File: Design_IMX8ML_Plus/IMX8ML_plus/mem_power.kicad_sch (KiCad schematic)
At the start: 22 parts

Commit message: processor capacitors location
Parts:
- removed C2 (x12): 1uF, Capacitor_SMD:C_0201_0603Metric_Pad0.64x0.40mm_HandSolder, symbol Device:C_Small
- removed C2 (x4): 10uF, Capacitor_SMD:C_0402_1005Metric, symbol Device:C_Small
- added C2 (x13): 1uF, Capacitor_SMD:C_0201_0603Metric_Pad0.64x0.40mm_HandSolder, symbol Device:C_Small
- added C2 (x3): 10uF, Capacitor_SMD:C_0402_1005Metric, symbol Device:C_Small
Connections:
- net GND: now also C2.2, C2.2, C2.2, C2.2, C2.2, C2.2, C2.2, C2.2, C2.2, C2.2, C2.2, C2.2, C2.2, C2.2, C2.2, C2.2
- net LPD4_VDD1 renamed VDD_1V8
- new net NVCC_DRAM_1V1: C2.1, C2.1, C2.1, C2.1, C2.1, C2.1, C2.1, C2.1, C2.1, C2.1, C2.1, C2.1, C2.1, C2.1, C2.1, C2.1

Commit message: Add SPB228 WIFI/BLE module
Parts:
- renumbered C2 to C124, C2 to C125, C2 to C126, C2 to C127, C2 to C128, C2 to C129, C2 to C130, C2 to C131, C2 to C133, C2 to C134, C2 to C135, C2 to C136, C2 to C137, C2 to C138, C2 to C139, C2 to C140, C2 to C3, C2 to C4, C2 to C5, C2 to C6, C2 to C7, C2 to C8

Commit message: [PROCESSOR] Create zones It added power zones in the four layer
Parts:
- renumbered C5 to C30, C4 to C31, C3 to C32, C6 to C33, C7 to C34, C8 to C35, C124 to C36, C125 to C37, C126 to C38, C127 to C39, C128 to C40, C129 to C41, C130 to C42, C131 to C43, C133 to C44, C134 to C45, C135 to C46, C136 to C47, C137 to C48, C138 to C49, C139 to C50, C140 to C51

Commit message: [IMX8ML-CPU] LPDDR4 memories reorganization of track between processor and memories.
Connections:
- net NVCC_DRAM_1V1 renamed LP4_VDD2
- net VDD_1V8 renamed LP4_VDD1
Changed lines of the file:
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@@
+	)
+	(junction
+		(at 96.52 58.42)
+		(diameter 0)
+		(color 0 0 0 0)
 	)
 	(junction
@@
 	)
 	(junction
+		(at 209.55 102.87)
+		(diameter 0)
+		(color 0 0 0 0)
+	)
+	(junction
 		(at 69.85 58.42)
 		(diameter 0)
@@
 	)
 	(junction
+		(at 209.55 81.28)
+		(diameter 0)
+		(color 0 0 0 0)
+	)
+	(junction
 		(at 173.99 81.28)
 		(diameter 0)
@@
 	(wire
 		(pts
+			(xy 209.55 81.28) (xy 214.63 81.28)
+		)
+		(stroke
+			(width 0)
+			(type default)
+		)
+	)
+	(wire
+		(pts
 			(xy 209.55 111.76) (xy 209.55 114.3)
 		)
@@
 	(wire
 		(pts
+			(xy 212.09 102.87) (xy 209.55 102.87)
+		)
+		(stroke
+			(width 0)
+			(type default)
+		)
+	)
+	(wire
+		(pts
 			(xy 96.52 67.31) (xy 96.52 69.85)
 		)
@@
 	(wire
 		(pts
+			(xy 99.06 58.42) (xy 96.52 58.42)
+		)
+		(stroke
+			(width 0)
+			(type default)
+		)
+	)
+	(wire
+		(pts
 			(xy 87.63 67.31) (xy 87.63 69.85)
 		)
@@
 		)
 	)
+	(global_label "LP4_VDDQ"
+		(shape input)
+		(at 212.09 102.87 0)
+		(fields_autoplaced yes)
+		(effects
+			(font
+				(size 1 1)
+			)
+			(justify left)
+		)
+		(property "Intersheetrefs" "${INTERSHEET_REFS}"
+			(at 221.8688 102.87 0)
+			(effects
+				(font
+					(size 1.27 1.27)
+				)
+				(justify left)
+				(hide yes)
+			)
+		)
+	)
+	(global_label "LP4_VDD1"
+		(shape input)
+		(at 99.06 58.42 0)
+		(fields_autoplaced yes)
+		(effects
+			(font
+				(size 1 1)
+			)
+			(justify left)
+		)
+		(property "Intersheetrefs" "${INTERSHEET_REFS}"
+			(at 108.7436 58.42 0)
+			(effects
+				(font
+					(size 1.27 1.27)
+				)
+				(justify left)
+				(hide yes)
+			)
+		)
+	)
+	(global_label "LP4_VDD2"
+		(shape input)
+		(at 214.63 81.28 0)
+		(fields_autoplaced yes)
+		(effects
+			(font
+				(size 1 1)
+			)
+			(justify left)
+		)
+		(property "Intersheetrefs" "${INTERSHEET_REFS}"
+			(at 224.3136 81.28 0)
+			(effects
+				(font
+					(size 1.27 1.27)
+				)
+				(justify left)
+				(hide yes)
+			)
+		)
+	)

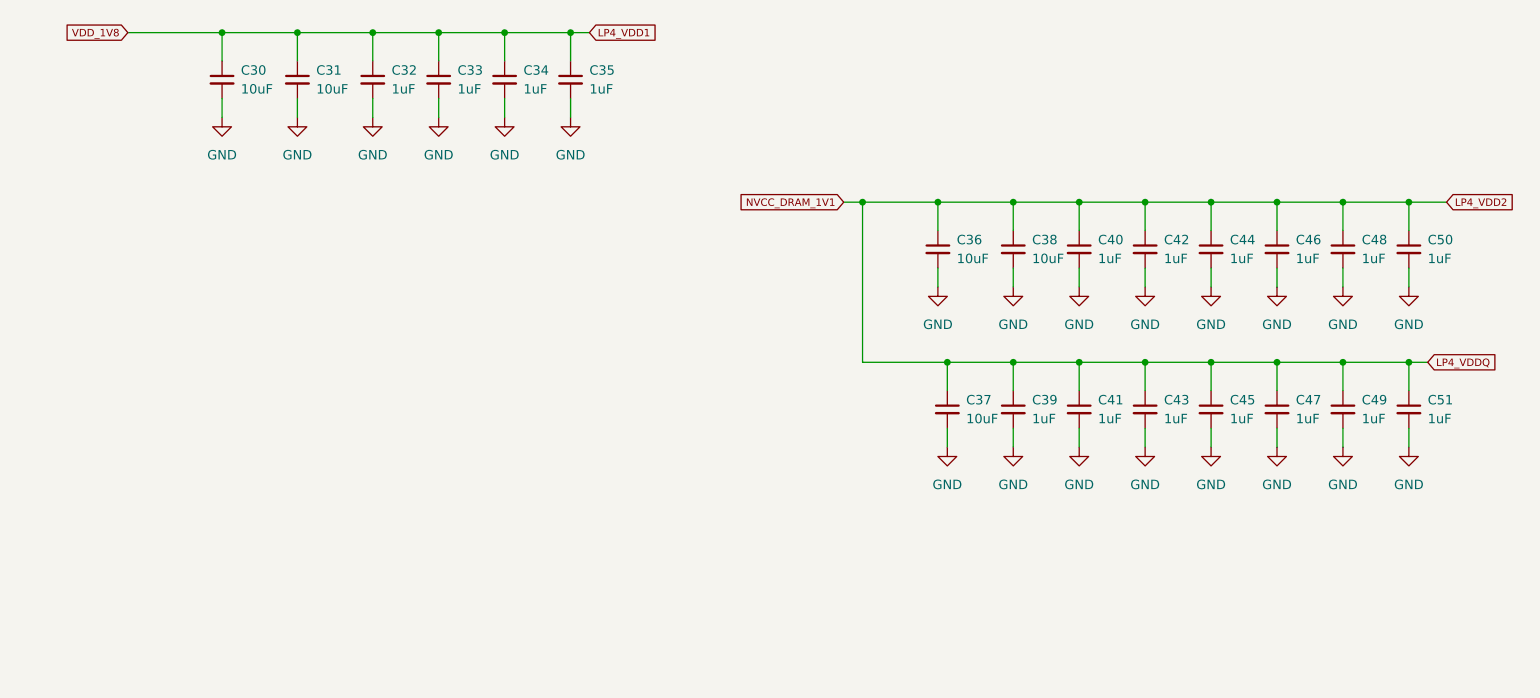
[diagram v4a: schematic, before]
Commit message: [BB_IMX8MLP IMX8MLP] Actuallizated to 9.0 kicad version
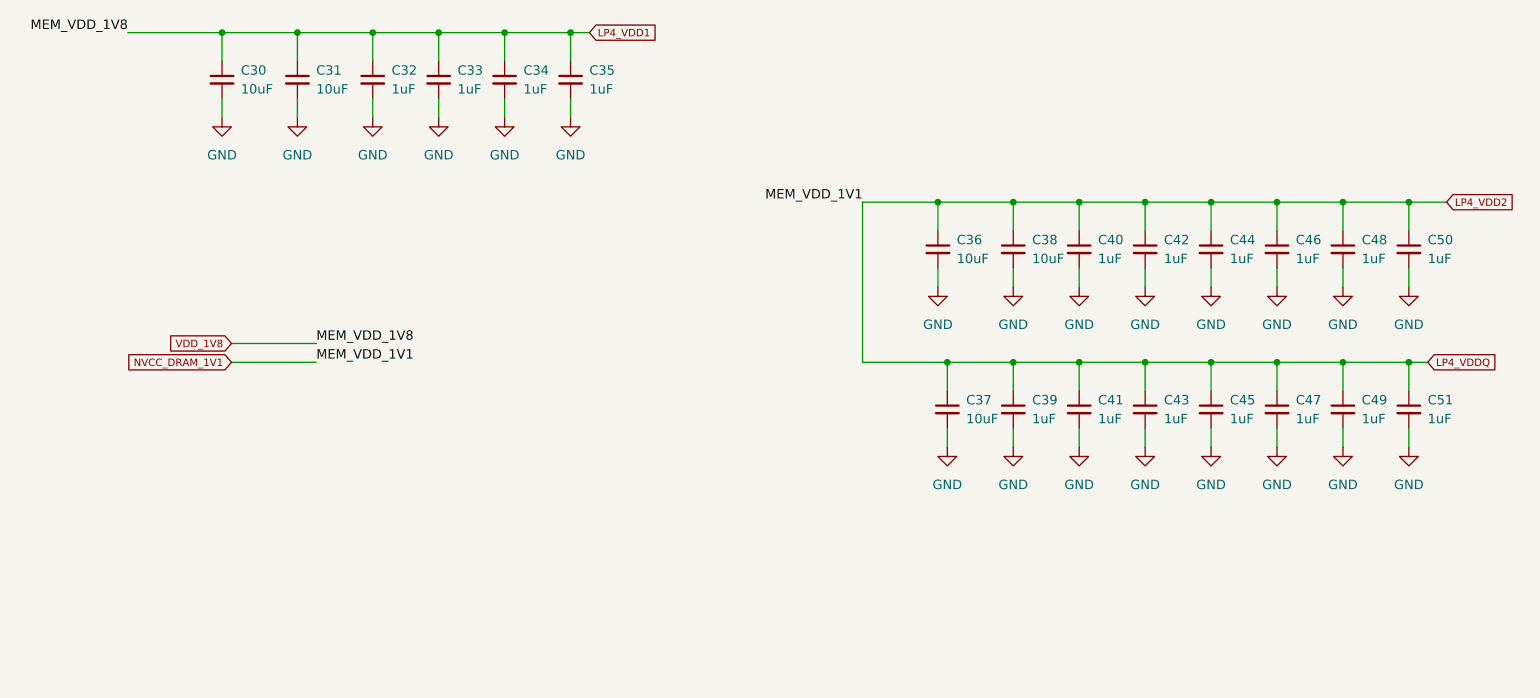
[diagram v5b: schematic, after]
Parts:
- C30, C31, C36, C37, C38: MP (none) -> CL05A106MQ5NUNC; Price (none) -> 0.1
- C32, C33, C34, C35, C39, C40, C41, C42, C43, C44, C45, C46, C47, C48, C49, C50, C51: footprint Capacitor_SMD:C_0201_0603Metric_Pad0.64x0.40mm_HandSolder -> Capacitor_SMD:C_0201_0603Metric; MP (none) -> 02016D105MAT2A; Price (none) -> 0.1
